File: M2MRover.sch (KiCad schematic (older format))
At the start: 9 parts

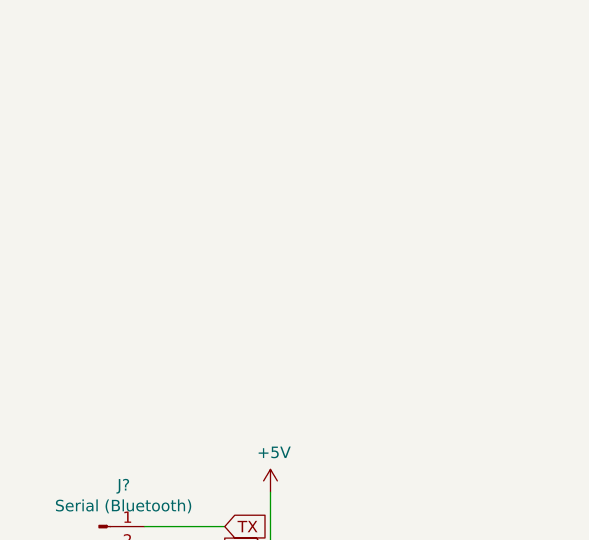
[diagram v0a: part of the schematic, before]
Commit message: Add connector for LDRs
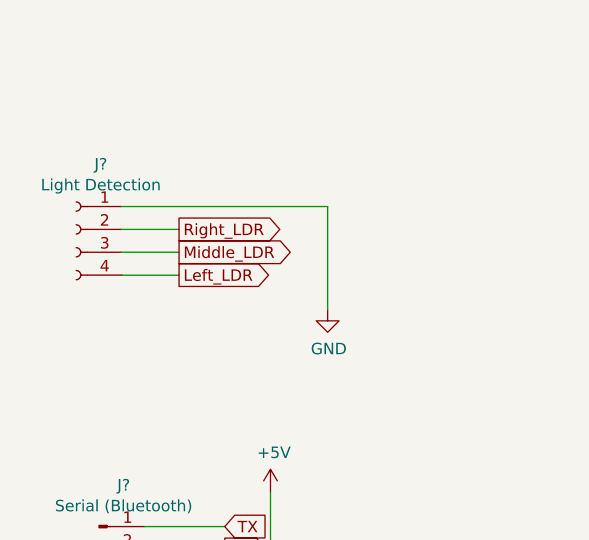
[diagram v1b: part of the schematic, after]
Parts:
- added J?: Light Detection, symbol Connector:Conn_01x04_Female
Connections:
- net GND: now also J?.1 (Pin_1)
- net Left_LDR: now also J?.4 (Pin_4)
- net Middle_LDR: now also J?.3 (Pin_3)
- net Right_LDR: now also J?.2 (Pin_2)
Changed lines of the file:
@@
 Wire Wire Line
 	7350 2050 7350 2200
+$Comp
+L Connector:Conn_01x04_Female J?
+U 1 1 5D730F79
+P 2000 1650
+F 0 "J?" H 1892 1935 50  0000 C CNN
+F 1 "Light Detection" H 1892 1844 50  0000 C CNN
+F 2 "" H 2000 1650 50  0001 C CNN
+F 3 "~" H 2000 1650 50  0001 C CNN
+	1    2000 1650
+	-1   0    0    -1
+$EndComp
+Text GLabel 2450 1650 2    50   Output ~ 0
+Right_LDR
+Text GLabel 2450 1750 2    50   Output ~ 0
+Middle_LDR
+Text GLabel 2450 1850 2    50   Output ~ 0
+Left_LDR
+$Comp
+L power:GND #PWR?
+U 1 1 5D7449E2
+P 3100 2000
+F 0 "#PWR?" H 3100 1750 50  0001 C CNN
+F 1 "GND" H 3105 1827 50  0000 C CNN
+F 2 "" H 3100 2000 50  0001 C CNN
+F 3 "" H 3100 2000 50  0001 C CNN
+	1    3100 2000
+	1    0    0    -1
+$EndComp
+Wire Wire Line
+	3100 2000 3100 1550
+Wire Wire Line
+	3100 1550 2200 1550
+Wire Wire Line
+	2200 1650 2450 1650
+Wire Wire Line
+	2450 1750 2200 1750
+Wire Wire Line
+	2200 1850 2450 1850
 $EndSCHEMATC

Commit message: Assign missing footprints to headers
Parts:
- J1, J5, J6, J8, J9: renamed from J?; footprint (none) -> Connector_PinSocket_2.54mm:PinSocket_1x04_P2.54mm_Vertical
- J4: renamed from J?; footprint (none) -> Connector_PinHeader_2.54mm:PinHeader_1x08_P2.54mm_Vertical
- gave numbers to parts that had none: 4
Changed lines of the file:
@@
 EESchema Schematic File Version 4
+LIBS:M2MRover-cache
 EELAYER 30 0
 EELAYER END
@@
 $EndDescr
 $Comp
-L MCU_Module:Arduino_Nano_v3.x A?
+L MCU_Module:Arduino_Nano_v3.x A1
 U 1 1 5D594B89
 P 5800 3750
-F 0 "A?" H 5800 2661 50  0000 C CNN
+F 0 "A1" H 5800 2661 50  0000 C CNN
 F 1 "Arduino_Nano_v3.x" H 5800 2570 50  0000 C CNN
 F 2 "Module:Arduino_Nano" H 5950 2800 50  0001 L CNN
@@
 	2850 3250 2850 3350
 $Comp
-L Connector:Conn_01x03_Male J?
+L Connector:Conn_01x03_Male J3
 U 1 1 5D5A7D2E
 P 2100 4350
-F 0 "J?" H 2208 4631 50  0000 C CNN
+F 0 "J3" H 2208 4631 50  0000 C CNN
 F 1 "Servo" H 2208 4540 50  0000 C CNN
 F 2 "Connector_PinHeader_2.54mm:PinHeader_1x03_P2.54mm_Vertical" H 2100 4350 50  0001 C CNN
@@
 $EndComp
 $Comp
-L Connector:Conn_01x04_Male J?
+L Connector:Conn_01x04_Male J2
 U 1 1 5D5A8825
 P 2100 3050
-F 0 "J?" H 2208 3331 50  0000 C CNN
+F 0 "J2" H 2208 3331 50  0000 C CNN
 F 1 "Serial (Bluetooth)" H 2208 3240 50  0000 C CNN
 F 2 "Connector_PinHeader_2.54mm:PinHeader_1x04_P2.54mm_Vertical" H 2100 3050 50  0001 C CNN
@@
 	2800 4250 2300 4250
 $Comp
-L Connector:Conn_01x04_Female J?
+L Connector:Conn_01x04_Female J7
 U 1 1 5D5B1217
 P 8950 3250
-F 0 "J?" H 8978 3226 50  0000 L CNN
+F 0 "J7" H 8978 3226 50  0000 L CNN
 F 1 "Compass GY-273" H 8978 3135 50  0000 L CNN
 F 2 "Connector_PinSocket_2.54mm:PinSocket_1x04_P2.54mm_Vertical" H 8950 3250 50  0001 C CNN
@@
 	6300 3750 6650 3750
 $Comp
-L Connector:Conn_01x08_Male J?
+L Connector:Conn_01x08_Male J4
 U 1 1 5D68405E
 P 2350 6000
-F 0 "J?" H 2458 6481 50  0000 C CNN
+F 0 "J4" H 2458 6481 50  0000 C CNN
 F 1 "H-Bridge" H 2458 6390 50  0000 C CNN
-F 2 "" H 2350 6000 50  0001 C CNN
+F 2 "Connector_PinHeader_2.54mm:PinHeader_1x08_P2.54mm_Vertical" H 2350 6000 50  0001 C CNN
 F 3 "~" H 2350 6000 50  0001 C CNN
 	1    2350 6000
@@
 $EndComp
 $Comp
-L power:+5V #PWR?
+L power:+5V #PWR0109
 U 1 1 5D68DE60
 P 2900 5400
-F 0 "#PWR?" H 2900 5250 50  0001 C CNN
+F 0 "#PWR0109" H 2900 5250 50  0001 C CNN
 F 1 "+5V" H 2915 5573 50  0000 C CNN
 F 2 "" H 2900 5400 50  0001 C CNN
@@
 $EndComp
 $Comp
-L power:GND #PWR?
+L power:GND #PWR0110
 U 1 1 5D691CCF
 P 3150 5950
-F 0 "#PWR?" H 3150 5700 50  0001 C CNN
+F 0 "#PWR0110" H 3150 5700 50  0001 C CNN
 F 1 "GND" H 3155 5777 50  0000 C CNN
 F 2 "" H 3150 5950 50  0001 C CNN
@@
 	3150 5700 3150 5950
 $Comp
-L Connector:Conn_01x04_Female J?
+L Connector:Conn_01x04_Female J8
 U 1 1 5D69DEA8
 P 9050 4650
-F 0 "J?" H 9078 4626 50  0000 L CNN
+F 0 "J8" H 9078 4626 50  0000 L CNN
 F 1 "Left Hall" H 9078 4535 50  0000 L CNN
-F 2 "" H 9050 4650 50  0001 C CNN
+F 2 "Connector_PinSocket_2.54mm:PinSocket_1x04_P2.54mm_Vertical" H 9050 4650 50  0001 C CNN
 F 3 "~" H 9050 4650 50  0001 C CNN
 	1    9050 4650
@@
 $EndComp
 $Comp
-L Connector:Conn_01x04_Female J?
+L Connector:Conn_01x04_Female J9
 U 1 1 5D69E9BA
 P 9050 5300
-F 0 "J?" H 9078 5276 50  0000 L CNN
+F 0 "J9" H 9078 5276 50  0000 L CNN
 F 1 "Right Hall" H 9078 5185 50  0000 L CNN
-F 2 "" H 9050 5300 50  0001 C CNN
+F 2 "Connector_PinSocket_2.54mm:PinSocket_1x04_P2.54mm_Vertical" H 9050 5300 50  0001 C CNN
 F 3 "~" H 9050 5300 50  0001 C CNN
 	1    9050 5300
@@
 $EndComp
 $Comp
-L power:+5V #PWR?
+L power:+5V #PWR0111
 U 1 1 5D69F1A3
 P 7900 4400
-F 0 "#PWR?" H 7900 4250 50  0001 C CNN
+F 0 "#PWR0111" H 7900 4250 50  0001 C CNN
 F 1 "+5V" H 7915 4573 50  0000 C CNN
 F 2 "" H 7900 4400 50  0001 C CNN
@@
 $EndComp
 $Comp
-L power:GND #PWR?
+L power:GND #PWR0112
 U 1 1 5D69F697
 P 8000 5600
-F 0 "#PWR?" H 8000 5350 50  0001 C CNN
+F 0 "#PWR0112" H 8000 5350 50  0001 C CNN
 F 1 "GND" H 8005 5427 50  0000 C CNN
 F 2 "" H 8000 5600 50  0001 C CNN
@@
 	8550 5500 8850 5500
 $Comp
-L Connector:Conn_01x04_Female J?
+L Connector:Conn_01x04_Female J5
 U 1 1 5D6DD620
 P 8950 1250
-F 0 "J?" H 8978 1226 50  0000 L CNN
+F 0 "J5" H 8978 1226 50  0000 L CNN
 F 1 "Ultrasonic Down" H 8978 1135 50  0000 L CNN
-F 2 "" H 8950 1250 50  0001 C CNN
+F 2 "Connector_PinSocket_2.54mm:PinSocket_1x04_P2.54mm_Vertical" H 8950 1250 50  0001 C CNN
 F 3 "~" H 8950 1250 50  0001 C CNN
 	1    8950 1250
@@
 $EndComp
 $Comp
-L Connector:Conn_01x04_Female J?
+L Connector:Conn_01x04_Female J6
 U 1 1 5D6DDAA8
 P 8950 1850
-F 0 "J?" H 8978 1826 50  0000 L CNN
+F 0 "J6" H 8978 1826 50  0000 L CNN
 F 1 "Ultrasonic Forward" H 8978 1735 50  0000 L CNN
-F 2 "" H 8950 1850 50  0001 C CNN
+F 2 "Connector_PinSocket_2.54mm:PinSocket_1x04_P2.54mm_Vertical" H 8950 1850 50  0001 C CNN
 F 3 "~" H 8950 1850 50  0001 C CNN
 	1    8950 1850
@@
 Ultrasonic_Forward_Echo
 $Comp
-L power:+5V #PWR?
+L power:+5V #PWR0113
 U 1 1 5D6E7CA7
 P 7450 950
-F 0 "#PWR?" H 7450 800 50  0001 C CNN
+F 0 "#PWR0113" H 7450 800 50  0001 C CNN
 F 1 "+5V" H 7465 1123 50  0000 C CNN
 F 2 "" H 7450 950 50  0001 C CNN
@@
 	8750 1850 8600 1850
 $Comp
-L power:GND #PWR?
+L power:GND #PWR0114
 U 1 1 5D6F22C6
 P 7350 2200
-F 0 "#PWR?" H 7350 1950 50  0001 C CNN
+F 0 "#PWR0114" H 7350 1950 50  0001 C CNN
 F 1 "GND" H 7355 2027 50  0000 C CNN
 F 2 "" H 7350 2200 50  0001 C CNN
@@
 	7350 2050 7350 2200
 $Comp
-L Connector:Conn_01x04_Female J?
+L Connector:Conn_01x04_Female J1
 U 1 1 5D730F79
 P 2000 1650
-F 0 "J?" H 1892 1935 50  0000 C CNN
+F 0 "J1" H 1892 1935 50  0000 C CNN
 F 1 "Light Detection" H 1892 1844 50  0000 C CNN
-F 2 "" H 2000 1650 50  0001 C CNN
+F 2 "Connector_PinSocket_2.54mm:PinSocket_1x04_P2.54mm_Vertical" H 2000 1650 50  0001 C CNN
 F 3 "~" H 2000 1650 50  0001 C CNN
 	1    2000 1650
@@
 Left_LDR
 $Comp
-L power:GND #PWR?
+L power:GND #PWR0115
 U 1 1 5D7449E2
 P 3100 2000
-F 0 "#PWR?" H 3100 1750 50  0001 C CNN
+F 0 "#PWR0115" H 3100 1750 50  0001 C CNN
 F 1 "GND" H 3105 1827 50  0000 C CNN
 F 2 "" H 3100 2000 50  0001 C CNN
